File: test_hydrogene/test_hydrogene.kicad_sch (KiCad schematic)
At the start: 15 parts, among them SW1 SW_Push, SW2 SW_Push, U3 STM32G474RBTx

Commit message: Fix diviseur de tension
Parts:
- R3: value 1.5K -> 6.8K
- R4: value 8.6K -> 3.6K
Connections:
- net +24V: now also U7.2 (VDC); no longer U7.
- net GND: now also U7.1 (GND); no longer U7.
- net at R4.1: now also U7.3 (SIG); no longer U7.
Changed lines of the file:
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@@
 		)
 	)
-	(text_box "Voltage divider to clamp 0-24 V from Transducer to 0-3.6 V for ADC pin\n"
+	(text_box "Voltage divider to clamp 0-5 V from Transducer to 0-3.3 V for ADC pin\n"
 		(exclude_from_sim no)
 		(at 217.424 16.256 0)
@@
 	)
 	(symbol
-		(lib_id "Transducer:SModel")
-		(at 237.49 27.94 0)
-		(mirror y)
-		(unit 1)
-		(exclude_from_sim no)
-		(in_bom yes)
-		(on_board yes)
-		(dnp no)
-		(property "Reference" "U7"
-			(at 237.49 27.178 0)
-			(effects
-				(font
-					(size 1.27 1.27)
-				)
-			)
-		)
-		(property "Value" "~"
-			(at 237.49 26.67 0)
-			(effects
-				(font
-					(size 1.27 1.27)
-				)
-			)
-		)
-		(property "Footprint" ""
-			(at 237.49 27.94 0)
-			(effects
-				(font
-					(size 1.27 1.27)
-				)
-				(hide yes)
-			)
-		)
-		(property "Datasheet" ""
-			(at 237.49 27.94 0)
-			(effects
-				(font
-					(size 1.27 1.27)
-				)
-				(hide yes)
-			)
-		)
-		(property "Description" ""
-			(at 237.49 27.94 0)
-			(effects
-				(font
-					(size 1.27 1.27)
-				)
-				(hide yes)
-			)
-		)
-		(pin ""
-		)
-		(pin ""
-		)
-		(pin ""
-		)
-		(pin ""
-		)
-		(instances
-			(project ""
-				(path "/1b141601-8b93-4745-b924-cd53eb4183d9"
-					(reference "U7")
-					(unit 1)
-				)
-			)
-		)
-	)
-	(symbol
 		(lib_id "power:GND")
 		(at 193.04 143.51 0)
@@
 			)
 		)
-		(property "Value" "1.5K"
+		(property "Value" "6.8K"
 			(at 226.06 48.26 90)
 			(effects
@@
 			)
 		)
-		(property "Value" "8.6K"
+		(property "Value" "3.6K"
 			(at 222.25 39.3699 0)
 			(effects
@@
 					(unit 1)
 				)
+			)
+		)
+	)
+	(symbol
+		(lib_id "Transducer:SModel")
+		(at 237.49 27.94 0)
+		(mirror y)
+		(unit 1)
+		(exclude_from_sim no)
+		(in_bom yes)
+		(on_board yes)
+		(dnp no)
+		(property "Reference" "U7"
+			(at 237.49 27.686 0)
+			(effects
+				(font
+					(size 1.27 1.27)
+				)
+			)
+		)
+		(property "Value" "~"
+			(at 237.49 26.67 0)
+			(effects
+				(font
+					(size 1.27 1.27)
+				)
+			)
+		)
+		(property "Footprint" ""
+			(at 237.49 27.94 0)
+			(effects
+				(font
+					(size 1.27 1.27)
+				)
+				(hide yes)
+			)
+		)
+		(property "Datasheet" ""
+			(at 237.49 27.94 0)
+			(effects
+				(font
+					(size 1.27 1.27)
+				)
+				(hide yes)
+			)
+		)
+		(property "Description" ""
+			(at 237.49 27.94 0)
+			(effects
+				(font
+					(size 1.27 1.27)
+				)
+				(hide yes)
+			)
+		)
+		(pin "3"
+		)
+		(pin "4"
+		)
+		(pin "1"
+		)
+		(pin "2"
+		)
+		(instances
+			(project ""
+				(path "/1b141601-8b93-4745-b924-cd53eb4183d9"
+					(reference "U7")
+					(unit 1)
+				)

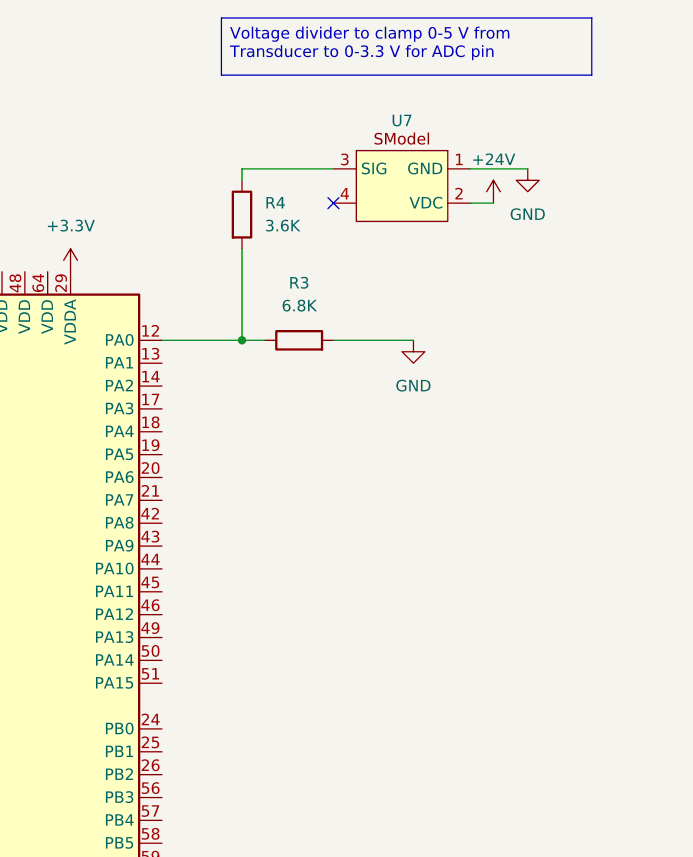
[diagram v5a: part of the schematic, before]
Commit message: Fix pour 2 manometres
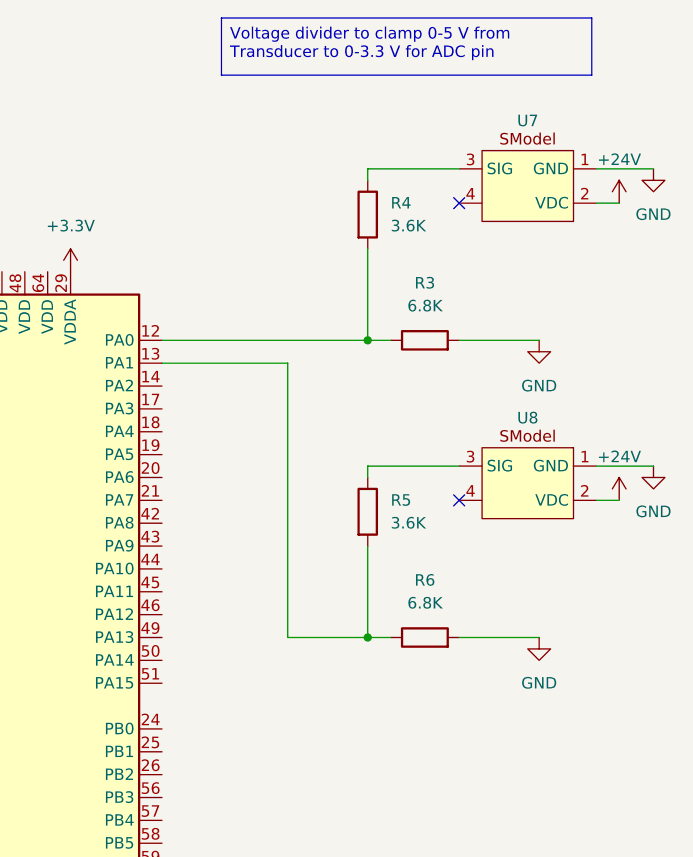
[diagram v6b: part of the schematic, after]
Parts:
- added R5: 3.6K, symbol Device:R
- added R6: 6.8K, symbol Device:R
- added U8: ~, symbol Transducer:SModel
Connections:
- net +24V: now also U8.2 (VDC)
- net GND: now also R6.2, U8.1 (GND)
- net at U3.13 (PA1): now also R5.2, R6.1
- new net: R5.1, U8.3 (SIG)
- no-connect marks 10 -> 11
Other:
- moved on the sheet: R3, R4, U7
